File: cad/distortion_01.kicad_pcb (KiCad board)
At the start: 2 copper layers, 54 x 99.8 mm, 105 parts, among them CON101 Ext_PSU, J101 JACK_IN, J102 JACK_OUT, P101 Battery_conn, P102 BYPASS_SWITCH, P103 CONN_01X03, P104 CONN_01X03, P105 CONN_01X03, P106 CONN_01X03, Q101 BS170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

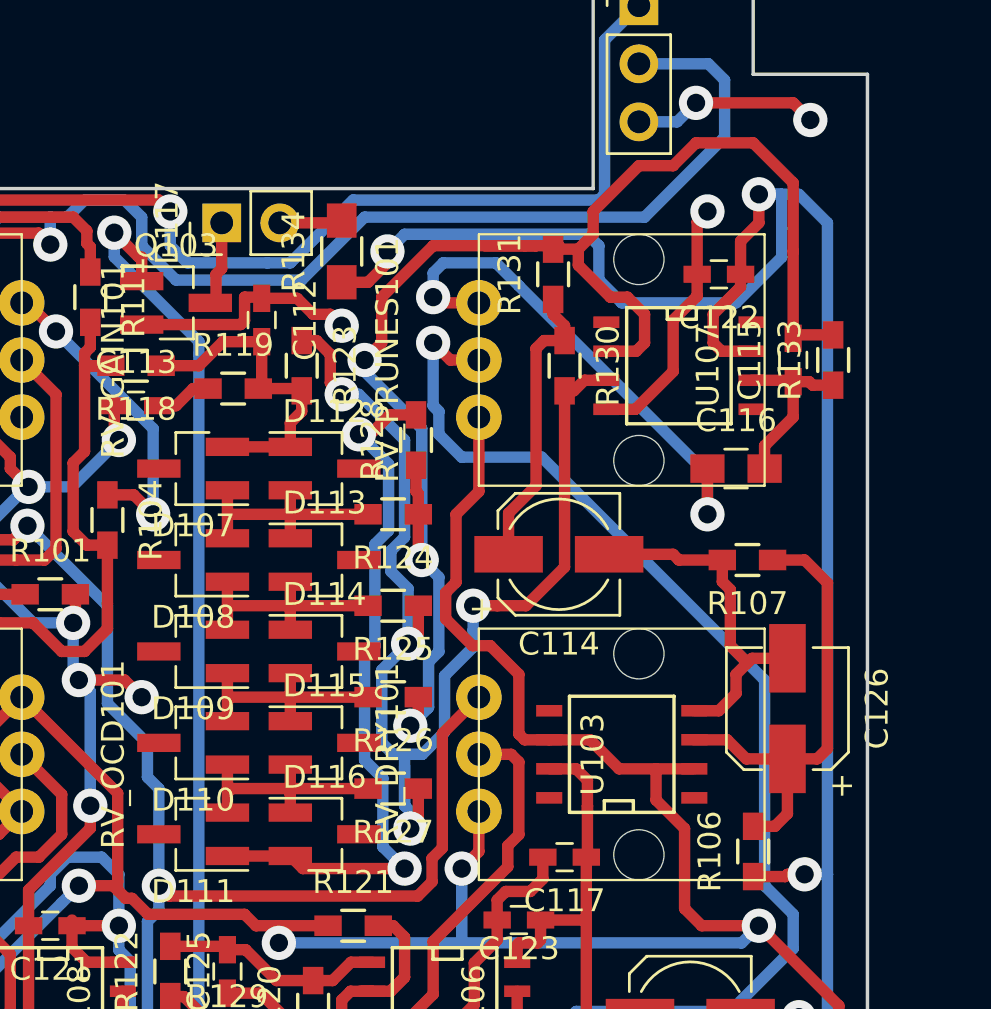
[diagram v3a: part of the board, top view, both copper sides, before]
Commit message: Added output capacitor on Prunes.
Changed capacitor value on octave output.
Corrected layout accordingly.
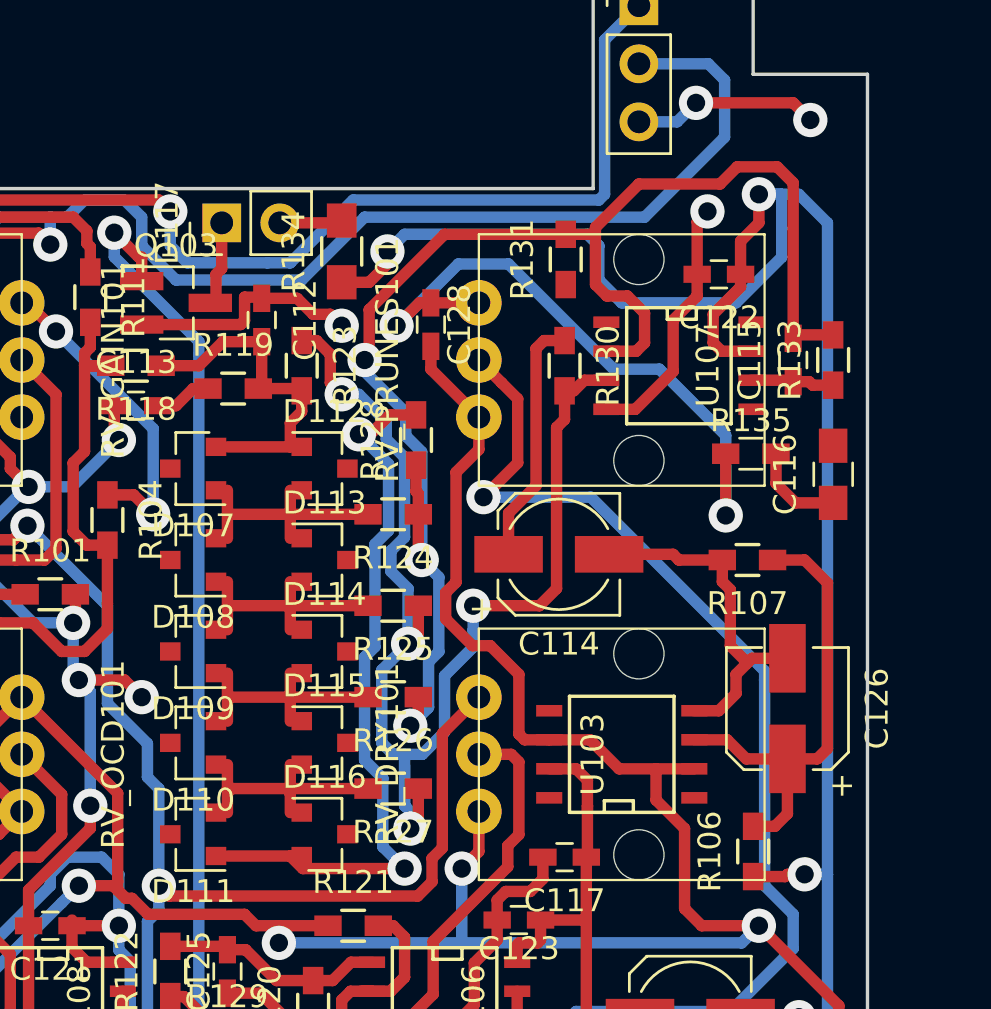
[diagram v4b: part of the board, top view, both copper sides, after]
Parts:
- added C128: 100n, Capacitors_SMD:C_0603_HandSoldering, F.Cu at (86.4, 72.0)
- added R135: 10k, Resistors_SMD:R_0603_HandSoldering, F.Cu at (100.4, 77.6)
- C127: value 10n -> 100n
- D107, D108, D109, D110, D111, D112, D113, D114, D115, D116: value D_Small -> BAS21; footprint TO_SOT_Packages_SMD:SOT-23_Handsoldering -> TO_SOT_Packages_SMD:SOT-23
- moved C116 4.26 mm to (104.0, 78.5), turned to 90 degrees
- moved R131 0.85 mm to (92.3, 69.1)
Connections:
- D107 pad 1: Net-(D107-Pad1) -> Net-(C112-Pad2)
- D107 pad 2: Net-(C112-Pad2) -> (no net)
- D107 pad 3: (no net) -> Net-(D107-Pad3)
- D108 pad 1: Net-(D108-Pad1) -> Net-(D107-Pad3)
- D108 pad 2: Net-(D107-Pad1) -> (no net)
- D108 pad 3: (no net) -> Net-(D108-Pad3)
- D109 pad 1: Net-(D109-Pad1) -> Net-(D108-Pad3)
- D109 pad 2: Net-(D108-Pad1) -> (no net)
- D109 pad 3: (no net) -> Net-(D109-Pad3)
- D110 pad 1: Net-(D110-Pad1) -> Net-(D109-Pad3)
- D110 pad 2: Net-(D109-Pad1) -> (no net)
- D110 pad 3: (no net) -> Net-(D110-Pad3)
- D111 pad 1: Net-(D111-Pad1) -> Net-(D110-Pad3)
- D111 pad 2: Net-(D110-Pad1) -> (no net)
- D111 pad 3: (no net) -> Net-(D111-Pad3)
- D112 pad 1: Net-(C112-Pad2) -> Net-(D107-Pad3)
- D112 pad 2: Net-(D107-Pad1) -> (no net)
- D112 pad 3: (no net) -> Net-(C112-Pad2)
- D113 pad 1: Net-(D107-Pad1) -> Net-(D108-Pad3)
- D113 pad 2: Net-(D108-Pad1) -> (no net)
- D113 pad 3: (no net) -> Net-(D107-Pad3)
- D114 pad 1: Net-(D108-Pad1) -> Net-(D109-Pad3)
- D114 pad 2: Net-(D109-Pad1) -> (no net)
- D114 pad 3: (no net) -> Net-(D108-Pad3)
- D115 pad 1: Net-(D109-Pad1) -> Net-(D110-Pad3)
- D115 pad 2: Net-(D110-Pad1) -> (no net)
- D115 pad 3: (no net) -> Net-(D109-Pad3)
- D116 pad 1: Net-(D110-Pad1) -> Net-(D111-Pad3)
- D116 pad 2: Net-(D111-Pad1) -> (no net)
- D116 pad 3: (no net) -> Net-(D110-Pad3)
- R124 pad 2: Net-(D107-Pad1) -> Net-(D107-Pad3)
- R125 pad 2: Net-(D108-Pad1) -> Net-(D108-Pad3)
- R126 pad 2: Net-(D109-Pad1) -> Net-(D109-Pad3)
- R127 pad 2: Net-(D110-Pad1) -> Net-(D110-Pad3)
- R128 pad 2: Net-(D111-Pad1) -> Net-(D111-Pad3)
- RV_PRUNES101 pad 1: Net-(C116-Pad1) -> Net-(C128-Pad1)
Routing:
- net Net-(D111-Pad3): track 0.00 -> 31.6 mm, vias 0 -> 2
- net Net-(D111-Pad1): track 31.6 -> 0.00 mm, vias 2 -> 0
- net Net-(C128-Pad1): track 0.00 -> 28.8 mm, vias 0 -> 2
- net Net-(C116-Pad1): track 22.9 -> 4.15 mm, vias 2 -> 0
- net Net-(D110-Pad3): track 0.00 -> 11.1 mm
- net Net-(D110-Pad1): track 11.1 -> 0.00 mm
- net Net-(D109-Pad3): track 0.00 -> 10.3 mm
- net Net-(D109-Pad1): track 10.3 -> 0.00 mm
- net Net-(D108-Pad3): track 0.00 -> 10.3 mm
- net Net-(D108-Pad1): track 10.3 -> 0.00 mm
- net Net-(D107-Pad3): track 0.00 -> 10.3 mm
- net Net-(D107-Pad1): track 10.3 -> 0.00 mm
- net Net-(C115-Pad1): track 7.98 -> 3.66 mm
- net VCOM: track 232.9 -> 236.9 mm
- net Net-(C115-Pad2): track 67.7 -> 64.0 mm
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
